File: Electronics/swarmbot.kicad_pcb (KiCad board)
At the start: 2 copper layers, 100 x 190 mm, 131 parts, among them J1 Front, J2 Top, J3 12x2 IDC, J4 12x2 IDC, J5 Conn_01x04_Male, J6 Battery 1S2P, J7 Raspberry_Pi_2_3, Q1 AO3400A, Q10 RSC002P03, Q2 Q_Photo_NPN_CE, Q3 Q_Photo_NPN_CE, Q4 Q_Photo_NPN_CE, Q5 Q_Photo_NPN_CE, Q6 Q_Photo_NPN_CE, Q7 BSH108, Q8 BSH108, Q9 BSH108, SW1 Left, SW2 Right, SW3 SW_SPST, U1 MPC17531A, U10 TP4056, U12 INA138, U13 AP2112K-3.3, U14 AP9101CK, U15 FDC6303N, U4 QRE1113GR, U5 QRE1113GR, U6 QRE1113GR, U7 QRE1113GR, U8 QRE1113GR, U9 ESP32-WROOM-32D

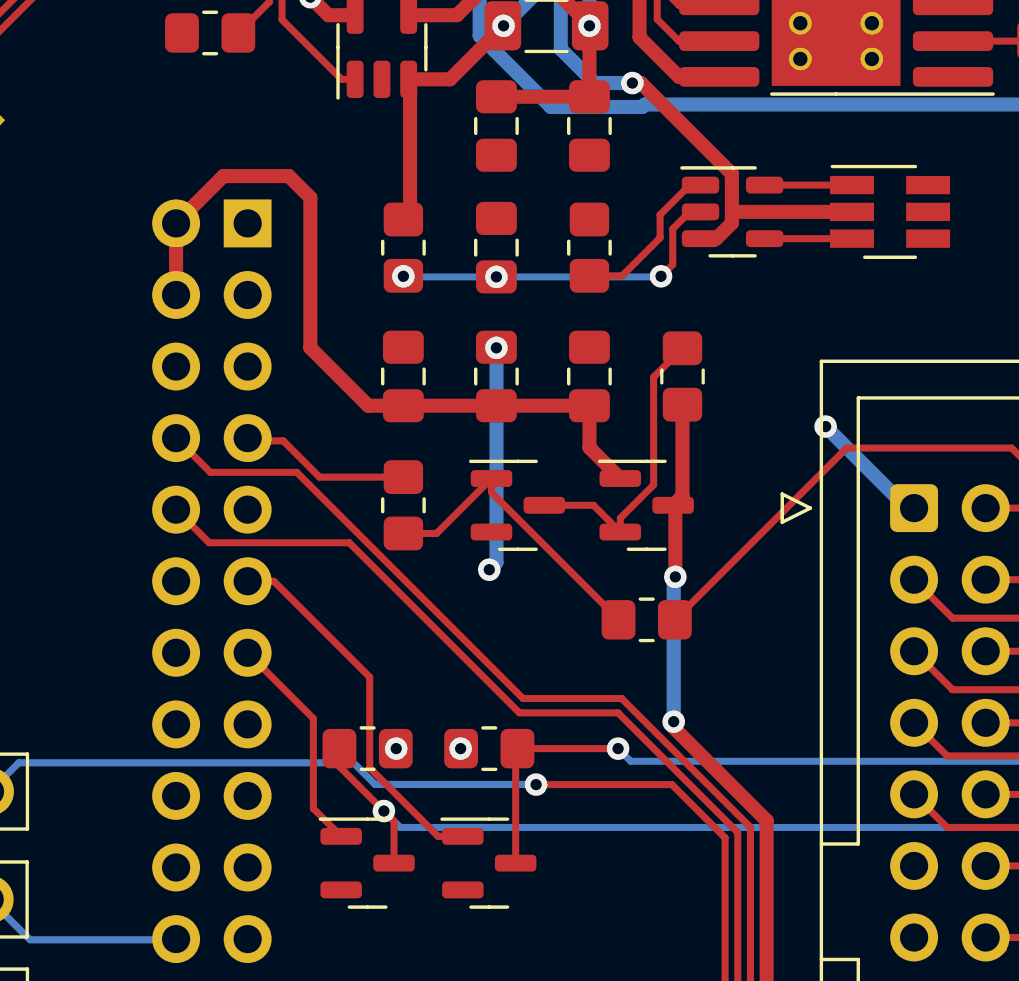
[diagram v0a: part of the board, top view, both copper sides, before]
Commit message: slight changes to layout
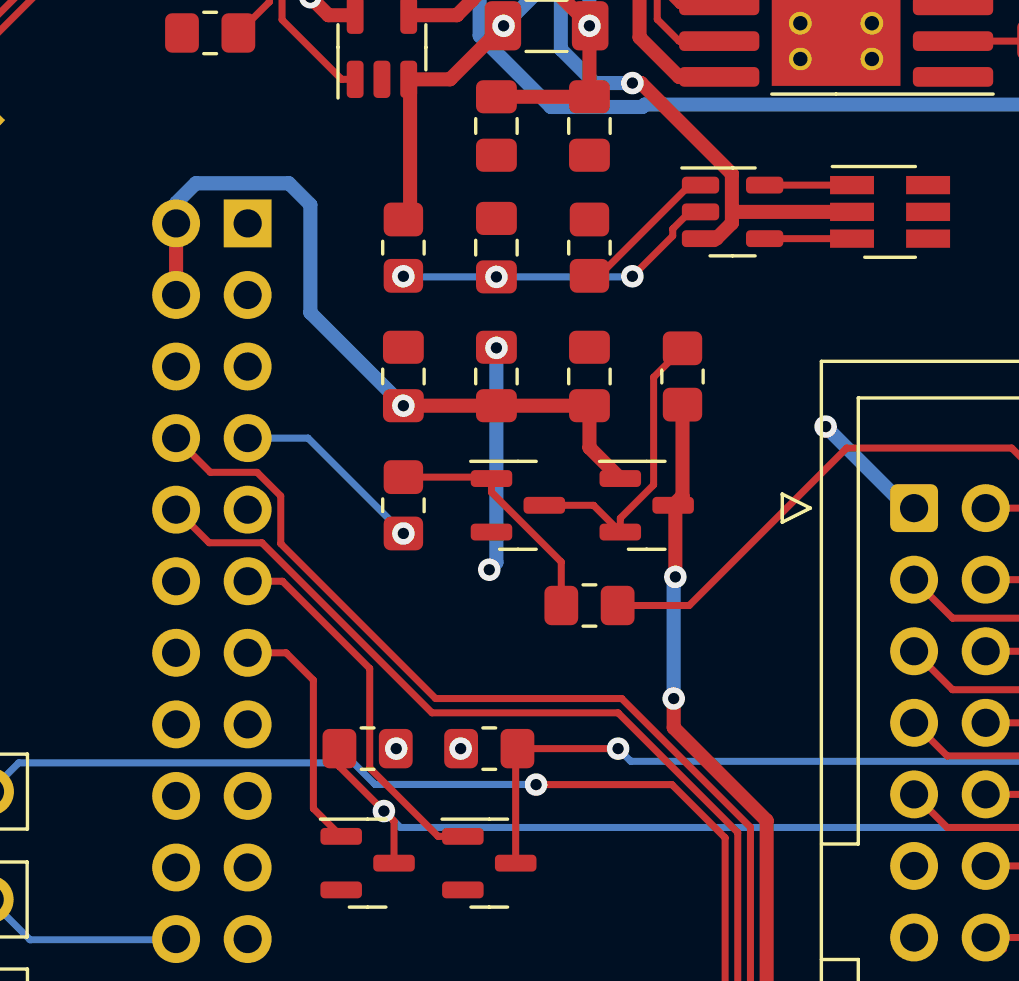
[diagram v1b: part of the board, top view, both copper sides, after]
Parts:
- moved R33 2.09 mm to (120.4, 139.4)
- turned R32 to -90 degrees
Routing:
- net Net-(Q9-Pad1): track 10.8 -> 8.68 mm
- net /Top PCB/ESP32/5V Switch 1: track 30.3 -> 32.1 mm
- net /Top PCB/ESP32/RX: track 74.8 -> 75.7 mm
- net /Top PCB/ESP32/5V Switch Aux: track 6.10 -> 7.02 mm, vias 0 -> 1
- net /Top PCB/ESP32/Flash: track 7.89 -> 8.69 mm
- net /Top PCB/ESP32/5V Switched 1: track 27.4 -> 26.8 mm, vias 0 -> 1
- net Net-(C25-Pad1): track 11.9 -> 11.3 mm
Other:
- board text added: "When re-importing changes to the PCB from the DXF file, the locations are X 120 Y 50, and X 120 Y 150. There should be two files, Edge Cuts, and User.2 per pcb. User.2 is used to help with alignment of components on the physical PCB."
- board text removed: "When re-importing changes to the PCB from the DXF file, the location is X 120 Y 50, and X 120 Y 150. There should be two files, Edge Cuts, and User.2 per pcb."

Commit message: don't use the enable pingit statusgit status
;
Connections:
- U9 pad 16: /Top PCB/ESP32/enable -> unconnected-(U9-Pad16)
- U9 pad 3: /Top PCB/ESP32/IR_1 -> /Top PCB/ESP32/enable
- U9 pad 4: /Top PCB/ESP32/IR_2 -> /Top PCB/ESP32/IR_1
- U9 pad 5: /Top PCB/ESP32/IR_3 -> /Top PCB/ESP32/IR_2
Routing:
- net /Top PCB/ESP32/enable: track 30.7 -> 47.1 mm
- net /Top PCB/ESP32/IR_LEDS: track 81.9 -> 77.2 mm
- net /Top PCB/ESP32/Bat I: track 19.1 -> 14.8 mm
- net /Top PCB/ESP32/Bat V: track 39.9 -> 35.7 mm
- net /Top PCB/ESP32/IR_5: track 173.0 -> 169.5 mm
- net /Top PCB/ESP32/IR_3: track 138.0 -> 135.0 mm
- net /Top PCB/ESP32/IR_4: track 154.1 -> 151.7 mm
- net /Top PCB/ESP32/IR_1: track 104.6 -> 105.4 mm
- net /Top PCB/ESP32/IR_2: track 121.0 -> 121.5 mm

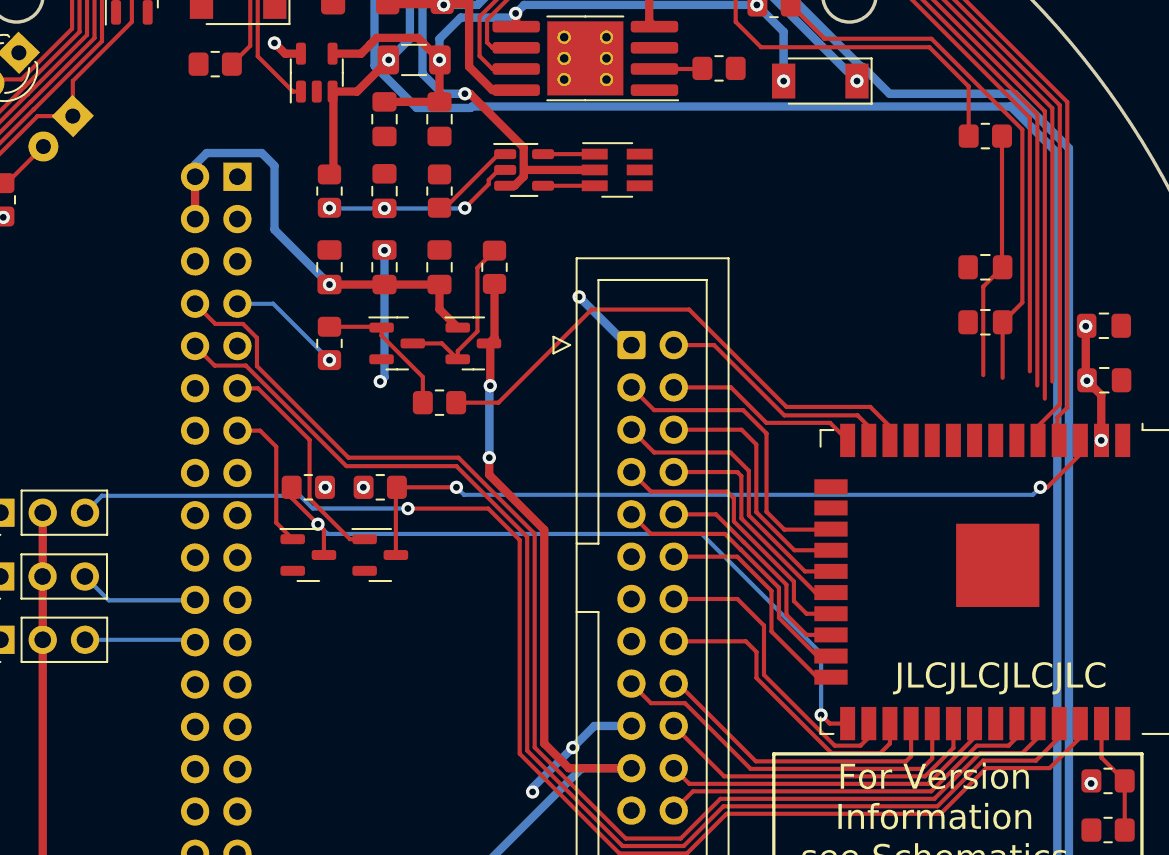
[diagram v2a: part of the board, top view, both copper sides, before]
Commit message: Fixed the enable pin being used
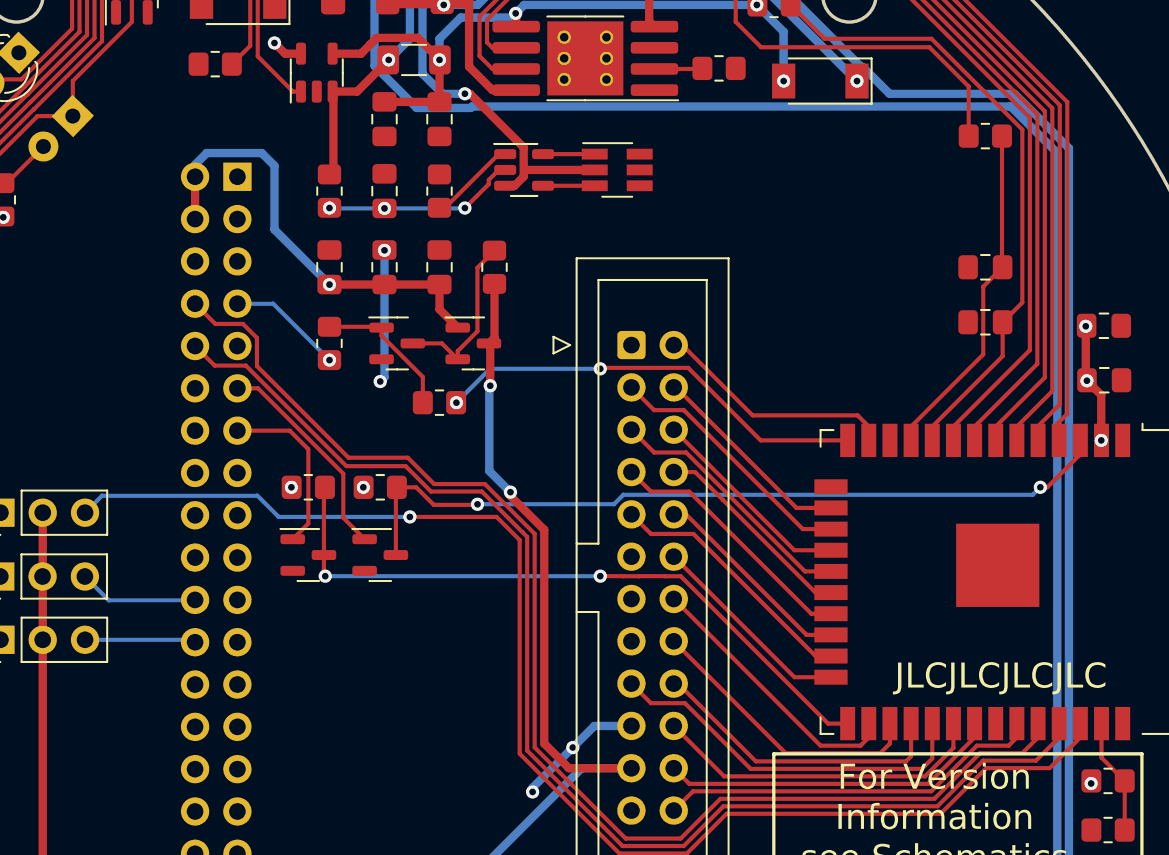
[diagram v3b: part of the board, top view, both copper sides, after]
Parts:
- turned R34 to 180 degrees
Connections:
- U9 pad 10: /Top PCB/ESP32/Bat I -> /Top PCB/ESP32/Bat V
- U9 pad 11: unconnected-(U9-Pad11) -> /Top PCB/ESP32/Bat I
- U9 pad 12: /Top PCB/ESP32/5V Switch 1 -> unconnected-(U9-Pad12)
- U9 pad 14: /Line Sensor 5 Top -> /Top PCB/ESP32/5V Switch 1
- U9 pad 16: unconnected-(U9-Pad16) -> /Line Sensor 5 Top
- U9 pad 6: /Top PCB/ESP32/IR_4 -> /Top PCB/ESP32/IR_3
- U9 pad 7: /Top PCB/ESP32/IR_5 -> /Top PCB/ESP32/IR_4
- U9 pad 8: /Top PCB/ESP32/IR_LEDS -> /Top PCB/ESP32/IR_5
- U9 pad 9: /Top PCB/ESP32/Bat V -> /Top PCB/ESP32/IR_LEDS
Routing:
- net /Top PCB/ESP32/IR_LEDS: track 77.2 -> 83.3 mm
- net /Top PCB/ESP32/5V Switch 1: track 32.1 -> 26.2 mm, vias 0 -> 2
- net /Top PCB/ESP32/Bat I: track 14.8 -> 20.5 mm
- net /Top PCB/ESP32/Bat V: track 35.7 -> 41.2 mm
- net /Top PCB/ESP32/IR_5: track 169.5 -> 174.3 mm
- net /Top PCB/ESP32/IR_3: track 135.0 -> 139.4 mm
- net GND: track 20.0 -> 15.9 mm, vias 5 -> 4
- net /Top PCB/ESP32/IR_4: track 151.7 -> 155.5 mm
- net /Top PCB/ESP32/program: track 43.8 -> 40.5 mm
- net /H-Bridge 1B Top: track 18.3 -> 15.5 mm
- net /Line Sensor LEDs Top: track 14.8 -> 12.4 mm
- net /Top PCB/ESP32/Flash: track 8.69 -> 10.5 mm
- net /Sonar Trigger Top: track 18.8 -> 17.0 mm
- net unconnected-(U9-Pad12): track 0.00 -> 1.66 mm
- net /H-Bridge 1A Top: track 18.0 -> 16.4 mm
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
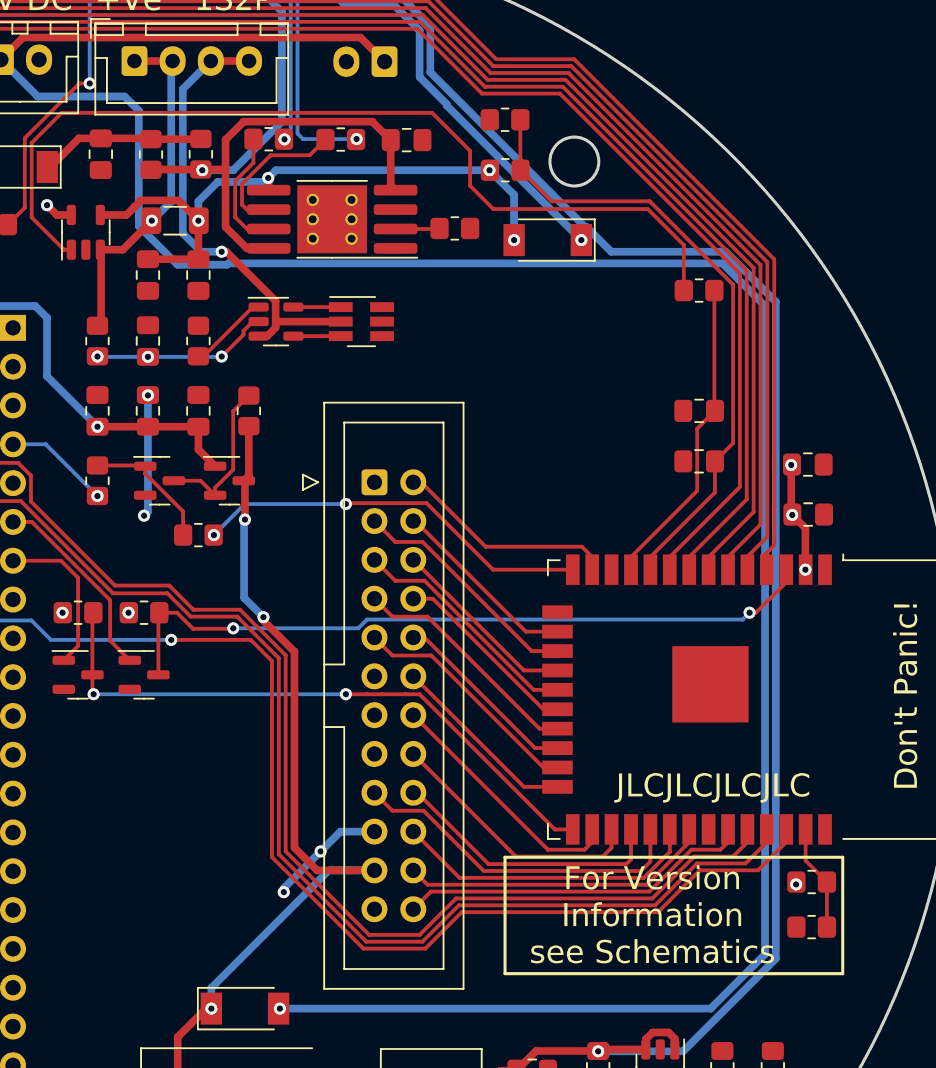
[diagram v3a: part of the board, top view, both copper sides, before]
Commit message: Cleaning up the stupid error with the pinout
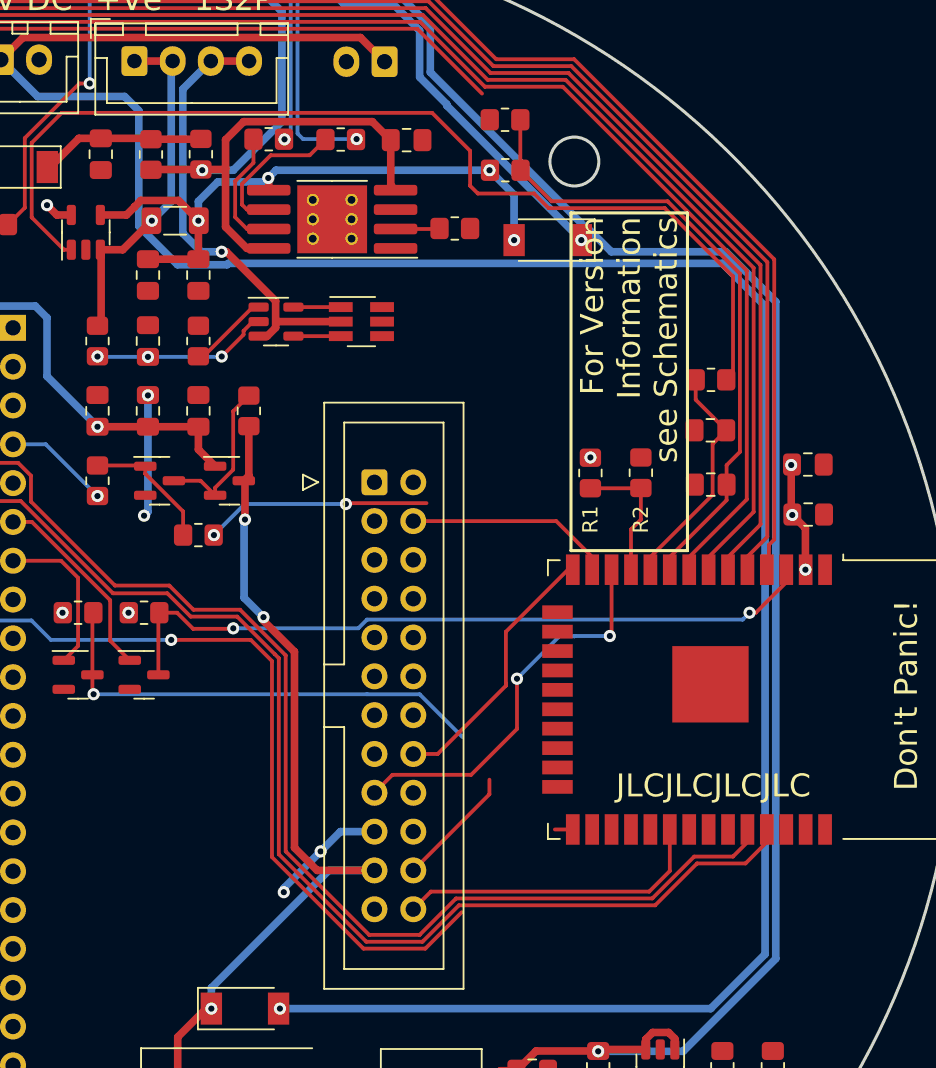
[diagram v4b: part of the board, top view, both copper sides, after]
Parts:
- moved R18 31.8 mm to (149.4, 135.4), turned to -90 degrees
- moved R17 30.4 mm to (146.1, 135.4), turned to 90 degrees
- moved R49 5.89 mm to (153.9, 129.3), turned to 0 degrees
- moved C20 1.70 mm to (153.9, 136.1)
- moved C23 1.47 mm to (153.9, 132.6)
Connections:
- U9 pad 10: /Top PCB/ESP32/Bat V -> /Top PCB/ESP32/Bat I
- U9 pad 11: /Top PCB/ESP32/Bat I -> /Top PCB/ESP32/Top PCB V
- U9 pad 12: unconnected-(U9-Pad12) -> /Bottom PCB V
- U9 pad 13: /Left Motor Sensor Top -> /Line Sensor 5 Top
- U9 pad 14: /Top PCB/ESP32/5V Switch 1 -> /Line Sensor 3 Top
- U9 pad 16: /Line Sensor 5 Top -> /Line Sensor 1 Top
- U9 pad 17: /H-Bridge 1B Top -> /H-Bridge 1A Top
- U9 pad 18: /Line Sensor LEDs Top -> /H-Bridge 1B Top
- U9 pad 19: /H-Bridge 1A Top -> /H-Bridge 2A Top
- U9 pad 20: /Left Switch Top -> /H-Bridge 2B Top
- U9 pad 21: /H-Bridge 2A Top -> /Left Switch Top
- U9 pad 22: /Line Sensor 4 Top -> /Line Sensor LEDs Top
- U9 pad 23: /H-Bridge 2B Top -> /Line Sensor 4 Top
- U9 pad 24: /Sonar Echo Top -> /Line Sensor 2 Top
- U9 pad 26: /Sonar Trigger Top -> /Top PCB/ESP32/IR_LEDS
- U9 pad 27: /Line Sensor 3 Top -> /Top PCB/Pen Servo
- U9 pad 28: /Line Sensor 2 Top -> /Left Motor Sensor Top
- U9 pad 29: /Bottom PCB V -> /Top PCB/ESP32/5V Switch 1
- U9 pad 30: /Right Switch Top -> /Right Motor Sensor Top
- U9 pad 31: /Line Sensor 1 Top -> /Sonar Echo Top
- U9 pad 33: /Right Motor Sensor Top -> /Sonar Trigger Top
- U9 pad 36: /Top PCB/Pen Servo -> /Right Switch Top
- U9 pad 37: /Top PCB/ESP32/Top PCB V -> unconnected-(U9-Pad37)
- U9 pad 9: /Top PCB/ESP32/IR_LEDS -> /Top PCB/ESP32/Bat V
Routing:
- net /Top PCB/ESP32/IR_LEDS: track 83.3 -> 41.1 mm
- net /Top PCB/Pen Servo: track 80.3 -> 56.3 mm
- net /Right Switch Top: track 19.4 -> 0.83 mm
- net /Line Sensor 2 Top: track 18.3 -> 0.31 mm
- net /H-Bridge 1A Top: track 16.4 -> 0.00 mm
- net /H-Bridge 2A Top: track 16.3 -> 0.00 mm
- net /Sonar Trigger Top: track 17.0 -> 1.47 mm
- net /H-Bridge 1B Top: track 15.5 -> 0.00 mm
- net /H-Bridge 2B Top: track 16.3 -> 0.83 mm
- net /Left Motor Sensor Top: track 14.6 -> 0.66 mm
- net /Sonar Echo Top: track 12.5 -> 0.01 mm
- net /Left Switch Top: track 13.3 -> 0.83 mm
- net /Line Sensor 4 Top: track 13.3 -> 0.83 mm
- net /Line Sensor 1 Top: track 19.6 -> 8.00 mm
- net /Line Sensor LEDs Top: track 12.4 -> 0.84 mm
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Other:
- board text added: "R1"
- board text added: "R2"
